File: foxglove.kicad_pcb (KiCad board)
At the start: 4 copper layers, 70.7 x 53.3 mm, 164 parts, among them IC1 LFE5U-12F-6BG256C, J1 NEIGHBOR1, J2 NEIGHBOR2, J3 Conn_02x05_Odd_Even, J4 Conn_02x10_Odd_Even, J5 Conn_01x02_Female, J6 Conn_02x03_Odd_Even, J7 BONUS_ROW, U1 LM393, U10 SHIFTER, U11 74HC4051, U12 SHIFTER, U13 74HC4051, U14 SHIFTER, U15 74HC4051, U16 SHIFTER, U17 74HC4051, U18 SHIFTER, U19 74HC4051, U2 ADP225, U20 SHIFTER, U21 74HC4051, U22 SHIFTER, U23 74HC4051, U24 SHIFTER, U25 74LVC1G53, U3 AP2127, U4 74LVC1G3157, U5 AP2127, U6 AP2127, U7 DAC084S085, U8 AT25xxx, U9 74HC4051

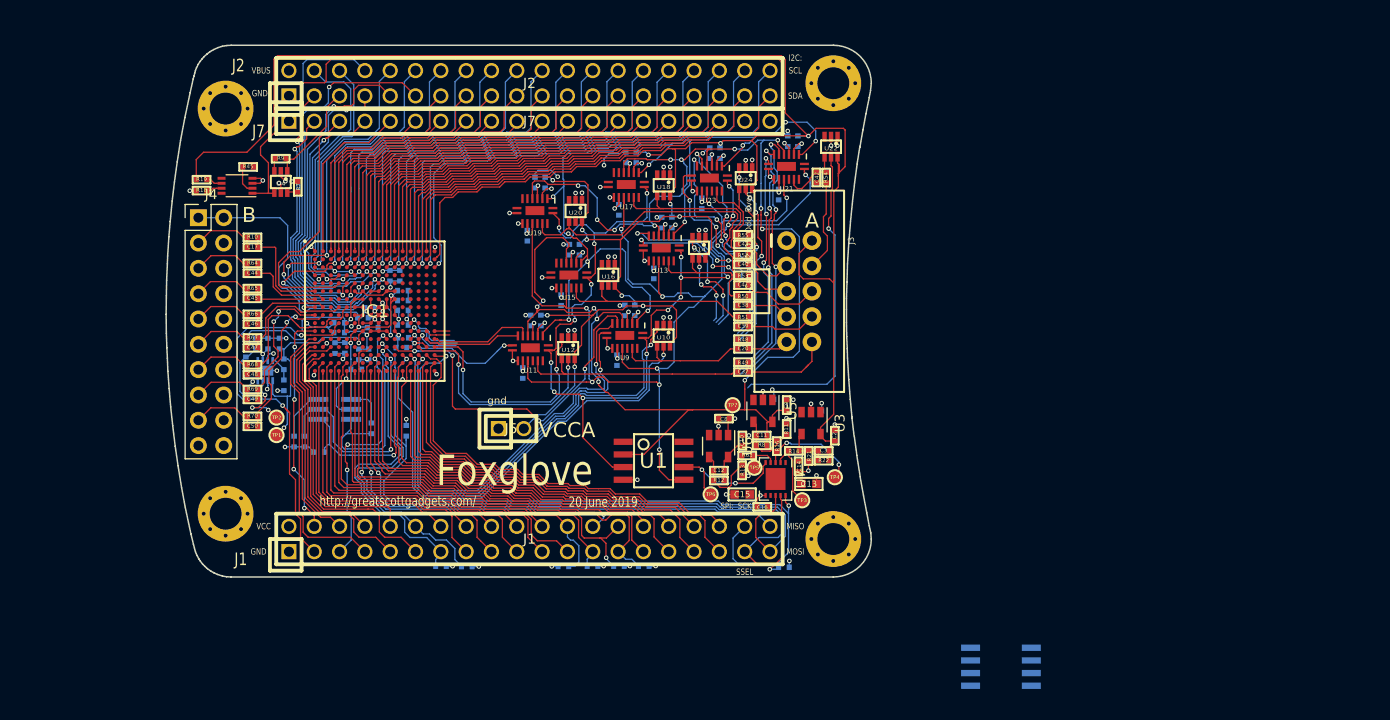
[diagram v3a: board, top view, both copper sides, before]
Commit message: Completed Bank A mux routing.
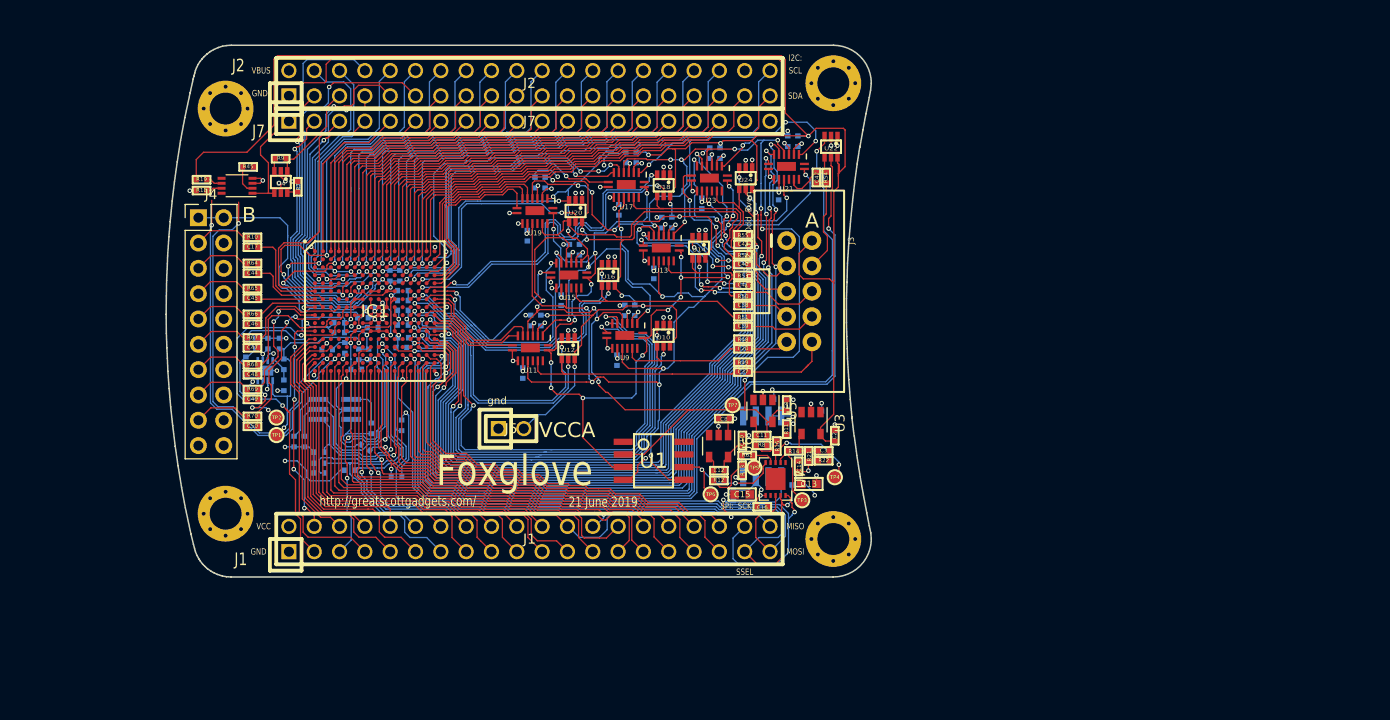
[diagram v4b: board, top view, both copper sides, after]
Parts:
- moved U8 32.6 mm to (169.4, 108.8), turned to 90 degrees
- moved R5 30.4 mm to (129.6, 108.9), turned to 325 degrees
- moved R6 29.0 mm to (125.0, 111.5), turned to 0 degrees
- moved R3 24.0 mm to (132.7, 111.9)
- moved R59 18.5 mm to (166.5, 113.7), turned to 270 degrees
- moved R57 16.0 mm to (125.0, 110.5), turned to 0 degrees
- moved R56 15.2 mm to (128.0, 111.2), turned to 0 degrees
- moved R15 8.36 mm to (172.9, 112.7)
- moved C25 0.80 mm to (125.8, 99.1), turned to 180 degrees
- moved R58 0.72 mm to (133.2, 106.7)
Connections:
- IC1 pad C15: /J2.38 -> /S0_5
- IC1 pad D12: Net-(IC1-PadD12) -> /S1_5
- IC1 pad D16: Net-(IC1-PadD16) -> /S0_6
- IC1 pad E12: Net-(IC1-PadE12) -> /S2_5
- IC1 pad E13: Net-(IC1-PadE13) -> /A6_shift
- IC1 pad E14: Net-(IC1-PadE14) -> /DIR_6
- IC1 pad E15: Net-(IC1-PadE15) -> /S1_6
- IC1 pad E16: Net-(IC1-PadE16) -> /S2_6
- IC1 pad F14: Net-(IC1-PadF14) -> /DIR_5
- IC1 pad F15: Net-(IC1-PadF15) -> /A5_shift
- IC1 pad F16: Net-(IC1-PadF16) -> /S2_4
- IC1 pad G13: Net-(IC1-PadG13) -> /A4_shift
- IC1 pad G14: Net-(IC1-PadG14) -> /S0_4
- IC1 pad G15: Net-(IC1-PadG15) -> /S1_4
- IC1 pad G16: Net-(IC1-PadG16) -> /S0_2
- IC1 pad H14: Net-(IC1-PadH14) -> /DIR_4
- IC1 pad H15: Net-(IC1-PadH15) -> /S1_2
- IC1 pad J13: Net-(IC1-PadJ13) -> /DIR_2
- IC1 pad J14: Net-(IC1-PadJ14) -> /A2_shift
- IC1 pad J15: Net-(IC1-PadJ15) -> /S2_2
- IC1 pad J16: Net-(IC1-PadJ16) -> /S2_1
- IC1 pad K13: /S0_3 -> /A3_shift
- IC1 pad K14: Net-(IC1-PadK14) -> /S0_1
- IC1 pad K15: Net-(IC1-PadK15) -> /S1_1
- IC1 pad K16: Net-(IC1-PadK16) -> /A1_shift
- IC1 pad L13: /S1_3 -> /S2_3
- IC1 pad L14: Net-(IC1-PadL14) -> /DIR_1
- IC1 pad L16: /A3_shift -> /S0_3
- IC1 pad M13: /S2_2 -> /S0_8
- IC1 pad M14: /S2_3 -> /S1_3
- IC1 pad M15: /S1_2 -> /S1_8
- IC1 pad M16: /S0_2 -> /S2_8
- IC1 pad N11: /S0_1 -> /S2_7
- IC1 pad N14: /DIR_2 -> /DIR_8
- IC1 pad N16: /A2_shift -> /A8_shift
- IC1 pad P12: /DIR_1 -> /DIR_7
- IC1 pad P13: /A1_shift -> /A7_shift
- IC1 pad P14: /S2_1 -> /S0_7
- IC1 pad P16: /S1_1 -> /S1_7
- J2 pad 38: /J2.38 -> Net-(J2-Pad38)
- R15 pad 1: +5V -> VCC
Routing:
- net /A7_shift: track 0.00 -> 89.6 mm, vias 0 -> 2
- net /S0_8: track 14.5 -> 85.4 mm, vias 3 -> 4
- net /S0_3: track 5.90 -> 75.1 mm, vias 1 -> 4
- net /S1_8: track 15.3 -> 81.7 mm, vias 3 -> 4
- net /DIR_8: track 17.0 -> 78.2 mm, vias 3 -> 4
- net /S2_7: track 23.5 -> 84.2 mm, vias 3 -> 4
- net /A3_shift: track 12.1 -> 71.9 mm, vias 3 -> 4
- net /A8_shift: track 18.5 -> 77.1 mm, vias 3 -> 4
- net /S2_8: track 21.4 -> 78.6 mm, vias 3 -> 4
- net /DIR_7: track 31.7 -> 88.0 mm, vias 1 -> 2
- net /S1_7: track 25.5 -> 81.7 mm, vias 3 -> 4
- net /DIR_3: track 10.1 -> 66.2 mm, vias 3 -> 4
- net /S1_3: track 21.2 -> 77.1 mm
- net /S2_3: track 22.0 -> 77.7 mm
- net /S0_7: track 26.7 -> 82.1 mm, vias 3 -> 4
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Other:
- board text added: "21 June 2019"
- board text removed: "20 June 2019"

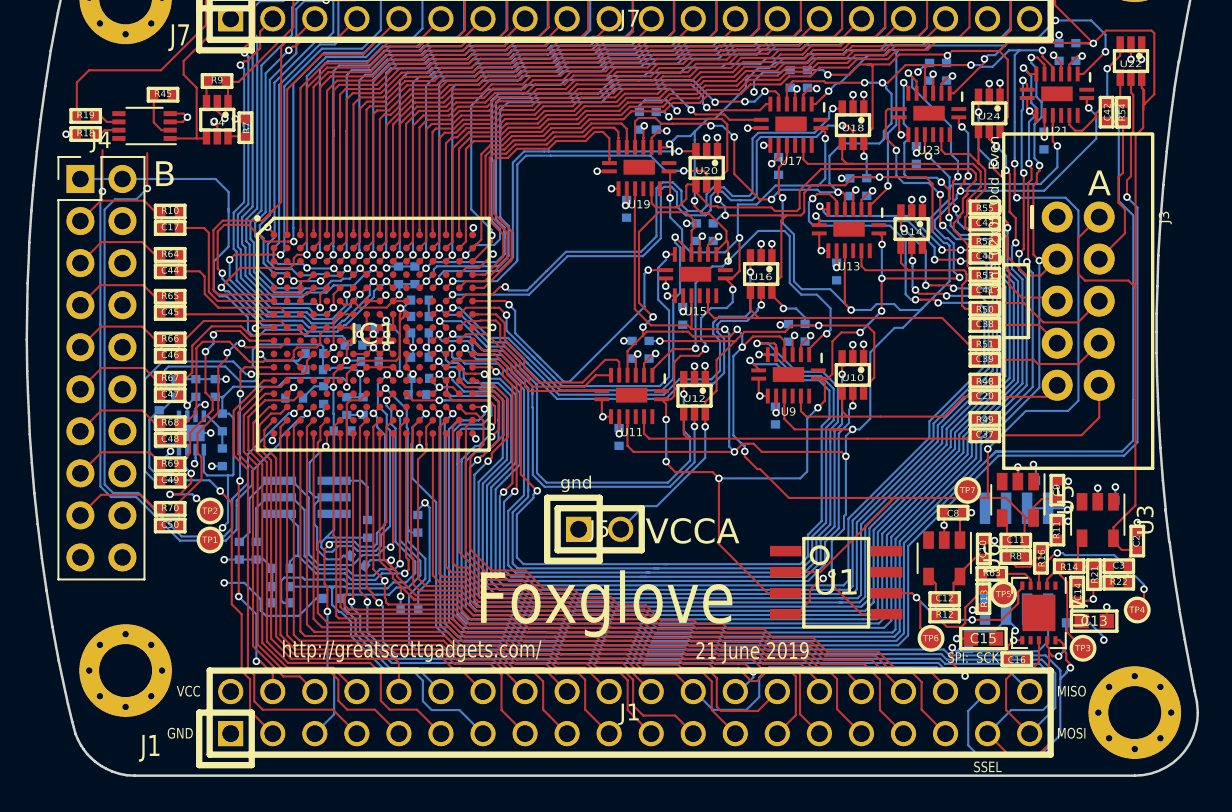
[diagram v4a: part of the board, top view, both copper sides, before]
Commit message: Added I2C IO expander
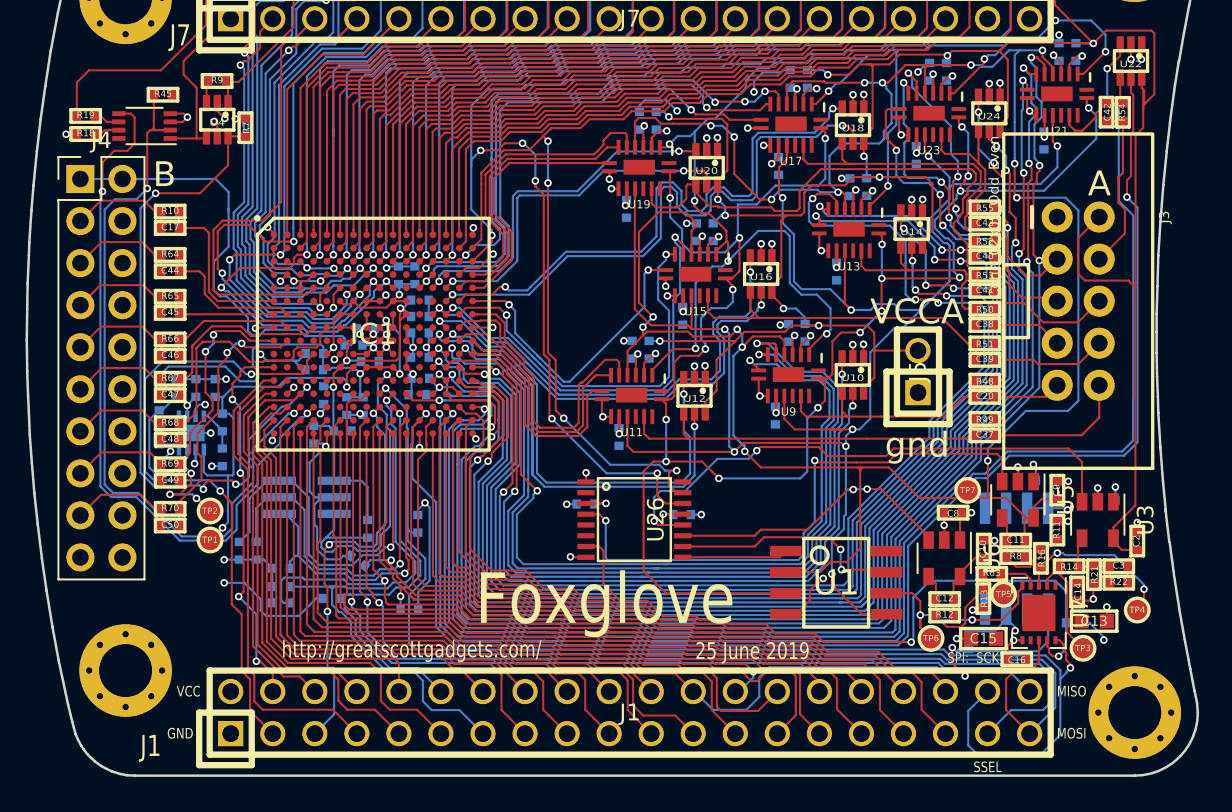
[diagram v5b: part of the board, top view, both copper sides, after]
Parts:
- added R71: 10k, gsg-modules:0402, B.Cu at (143.3, 105.5)
- added R72: 10k, gsg-modules:0402, B.Cu at (149.2, 106.1)
- added U26: PCA6408A, gsg-modules:TSSOP16, F.Cu at (146.3, 106.5)
- moved J5 21.5 mm to (163.4, 97.5), turned to 90 degrees
- moved C25 2.51 mm to (126.9, 101.3), turned to 270 degrees
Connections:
- IC1 pad M3: Net-(IC1-PadM3) -> /div_en
- IC1 pad P3: Net-(IC1-PadP3) -> /pull_en
- IC1 pad P4: Net-(IC1-PadP4) -> /pull_sel
- R15 pad 1: VCC -> +5V
- R15 pad 2: /SSEL -> /DAC~SYNC~
- R7 pad 1: /div_sel -> /div_en
- U4 pad 6: /div_sel -> /div_en
- U7 pad 9: /SSEL -> /DAC~SYNC~
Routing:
- net /pull_sel: track 0.00 -> 44.0 mm, vias 0 -> 2
- net /pull_en: track 2.93 -> 45.5 mm, vias 0 -> 2
- net /DAC~SYNC~: track 0.00 -> 41.5 mm, vias 0 -> 2
- net /div_en: track 0.00 -> 40.4 mm, vias 0 -> 4
- net Net-(IC1-PadP3): track 40.3 -> 0.00 mm, vias 2 -> 0
- net Net-(IC1-PadP4): track 39.7 -> 0.00 mm, vias 2 -> 0
- net /DAC2_EN: track 0.00 -> 34.8 mm, vias 0 -> 2
- net /VCCA_EN: track 0.00 -> 33.5 mm, vias 0 -> 2
- net /J2.40: track 51.0 -> 83.2 mm, vias 1 -> 6
- net /J2.39: track 44.7 -> 72.0 mm, vias 0 -> 4
- net /VCCB_EN: track 0.00 -> 17.4 mm, vias 0 -> 2
- net /COUT2: track 0.00 -> 14.1 mm, vias 0 -> 2
- net /SSEL: track 75.4 -> 61.8 mm, vias 2 -> 1
- net /DIR_2: track 27.1 -> 35.2 mm
- net /COMP1: track 103.1 -> 110.5 mm
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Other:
- board text added: "25 June 2019"
- board text removed: "21 June 2019"

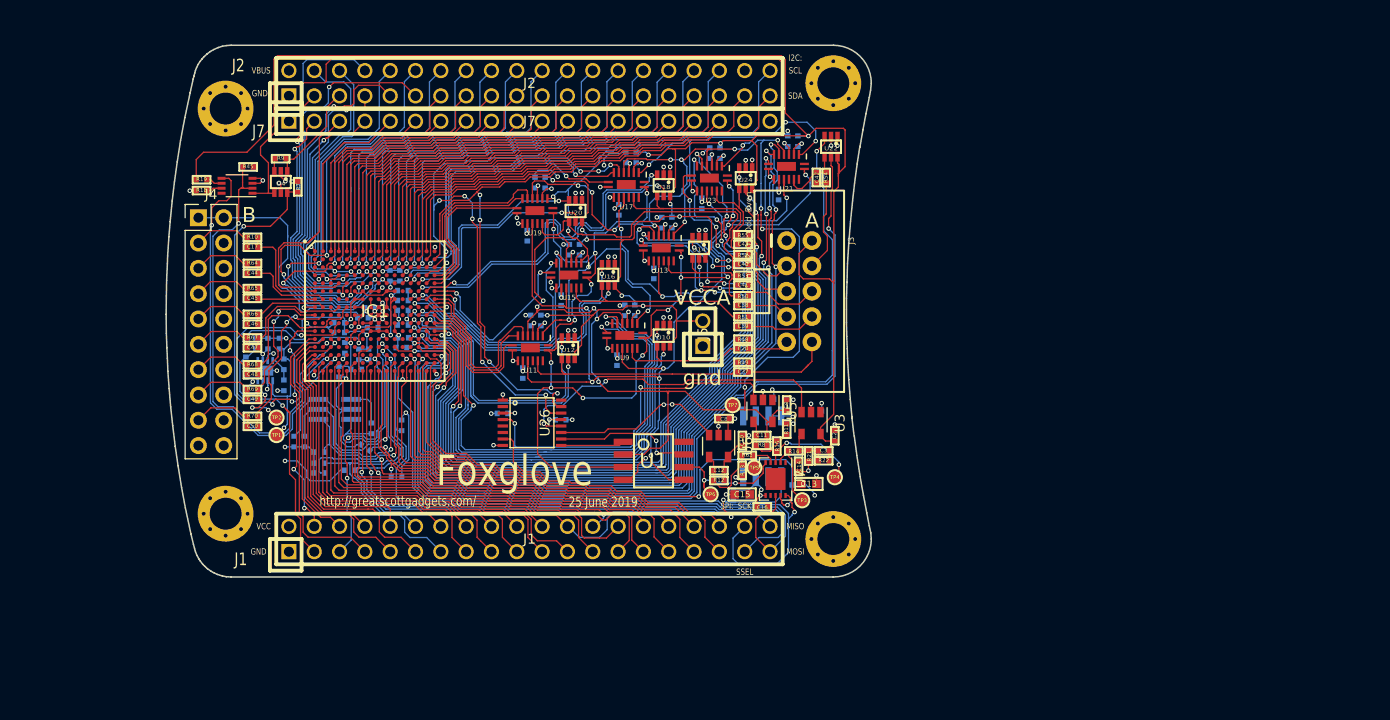
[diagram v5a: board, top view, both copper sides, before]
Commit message: Completed routing
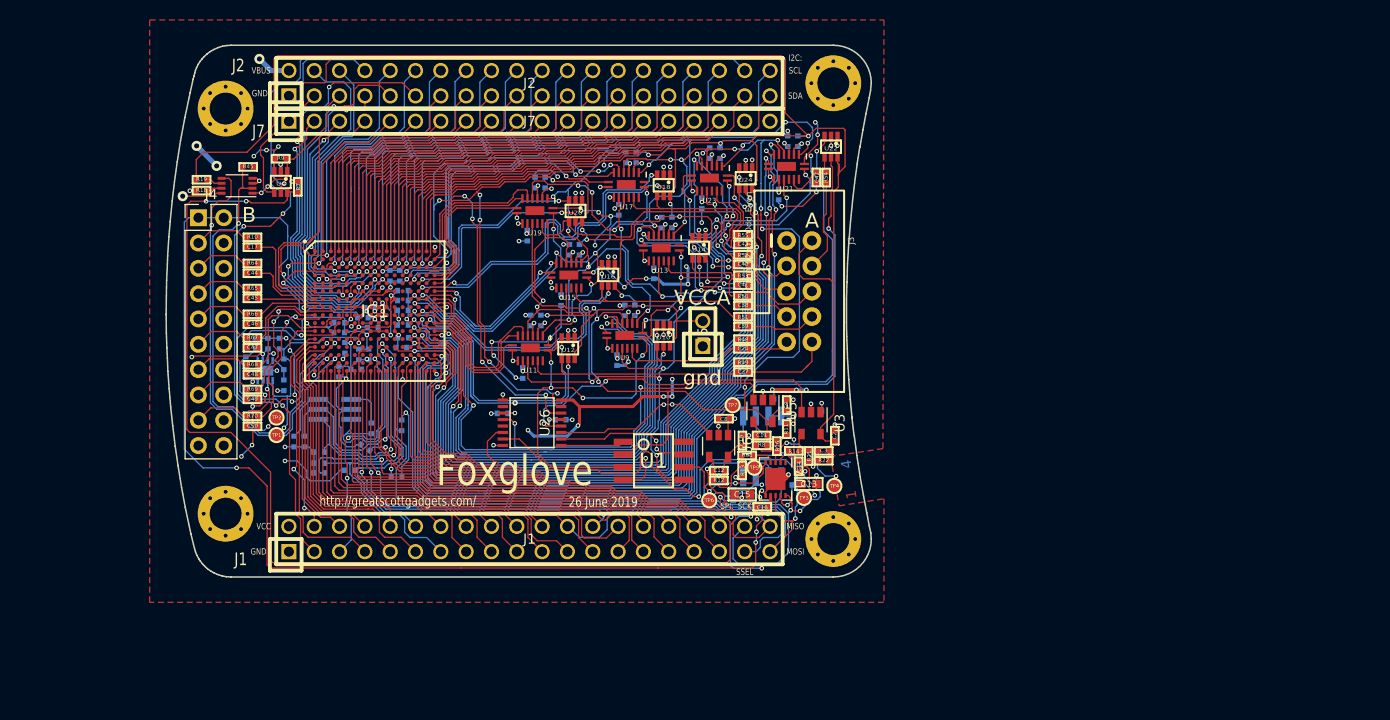
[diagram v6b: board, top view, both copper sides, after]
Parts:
- moved TP4 0.88 mm to (176.6, 112.8)
- moved TP6 0.61 mm to (164.1, 114.2)
- moved TP3 0.30 mm to (173.6, 114.0)
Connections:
- IC1 pad F6: /VCCIO0 -> VCC
- IC1 pad F7: /VCCIO0 -> VCC
- IC1 pad M3: /div_en -> /J2.38
- J2 pad 38: Net-(J2-Pad38) -> /J2.38
- U26 pad 6: Net-(U26-Pad6) -> /div_en
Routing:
- net +5V: track 7.33 -> 150.6 mm, vias 6 -> 52
- net /VCCB: track 33.7 -> 141.9 mm, vias 1 -> 6
- net /J2.38: track 0.00 -> 101.4 mm, vias 0 -> 5
- net /div_en: track 40.4 -> 136.3 mm, vias 4 -> 2
- net /MISO: track 54.2 -> 74.2 mm, vias 1 -> 2
- net /MOSI: track 66.3 -> 82.4 mm, vias 1 -> 2
- net /SCK: track 75.1 -> 89.3 mm, vias 2 -> 3
- net GND: track 116.9 -> 124.2 mm, vias 74 -> 78
- net /S1_4: track 24.1 -> 18.3 mm
- net /S0_4: track 26.5 -> 21.0 mm
- net /ADC: track 10.4 -> 15.3 mm, vias 0 -> 2
- net /S1_8: track 81.7 -> 84.4 mm
- net /DAC~SYNC~: track 41.5 -> 43.8 mm
- net /S2_8: track 78.6 -> 80.9 mm
- net /ADC_A: track 161.1 -> 159.1 mm
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- added copper zone on F.Cu, net +5V
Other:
- board text added: "1"
- board text added: "26 June 2019"
- board text added: "4"
- board text removed: "25 June 2019"
